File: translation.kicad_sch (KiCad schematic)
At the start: 12 parts, among them Q1 DMG1013UW-7, Q2 DMG1012UW-7, Q3 DMG1012UW-7, U3 TC1262-3.0VDBTR, U4 FXLA108BQX

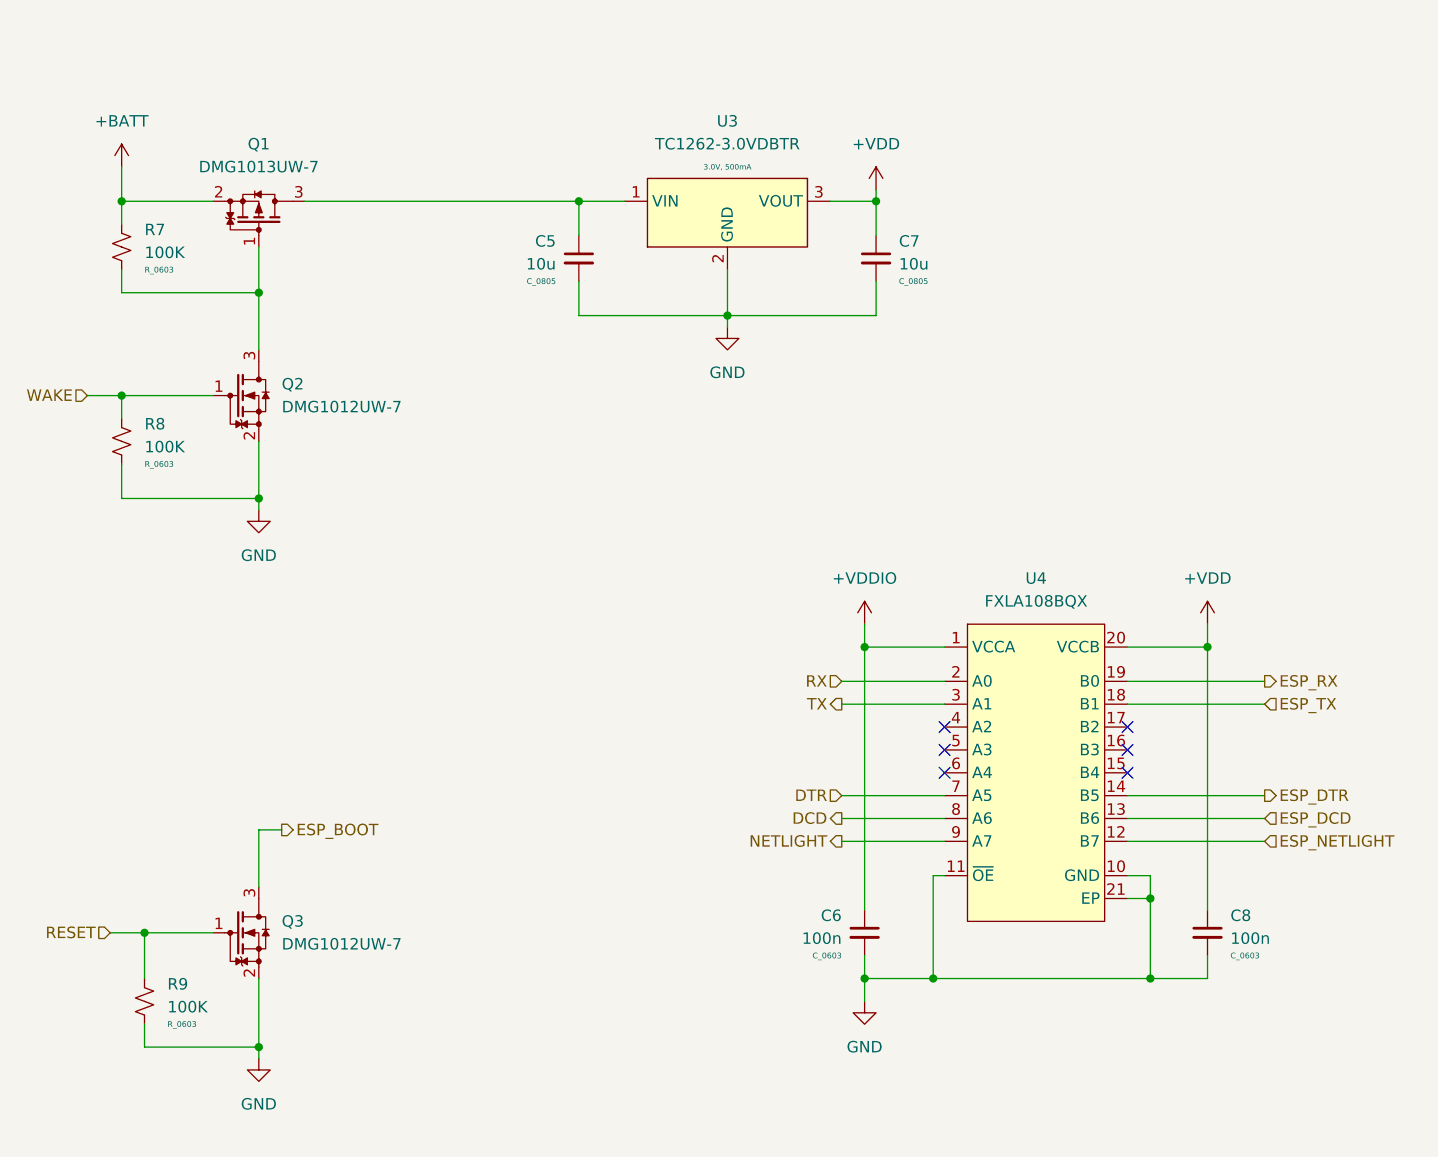
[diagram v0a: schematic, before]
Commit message: Overhaul for buck-boost converter
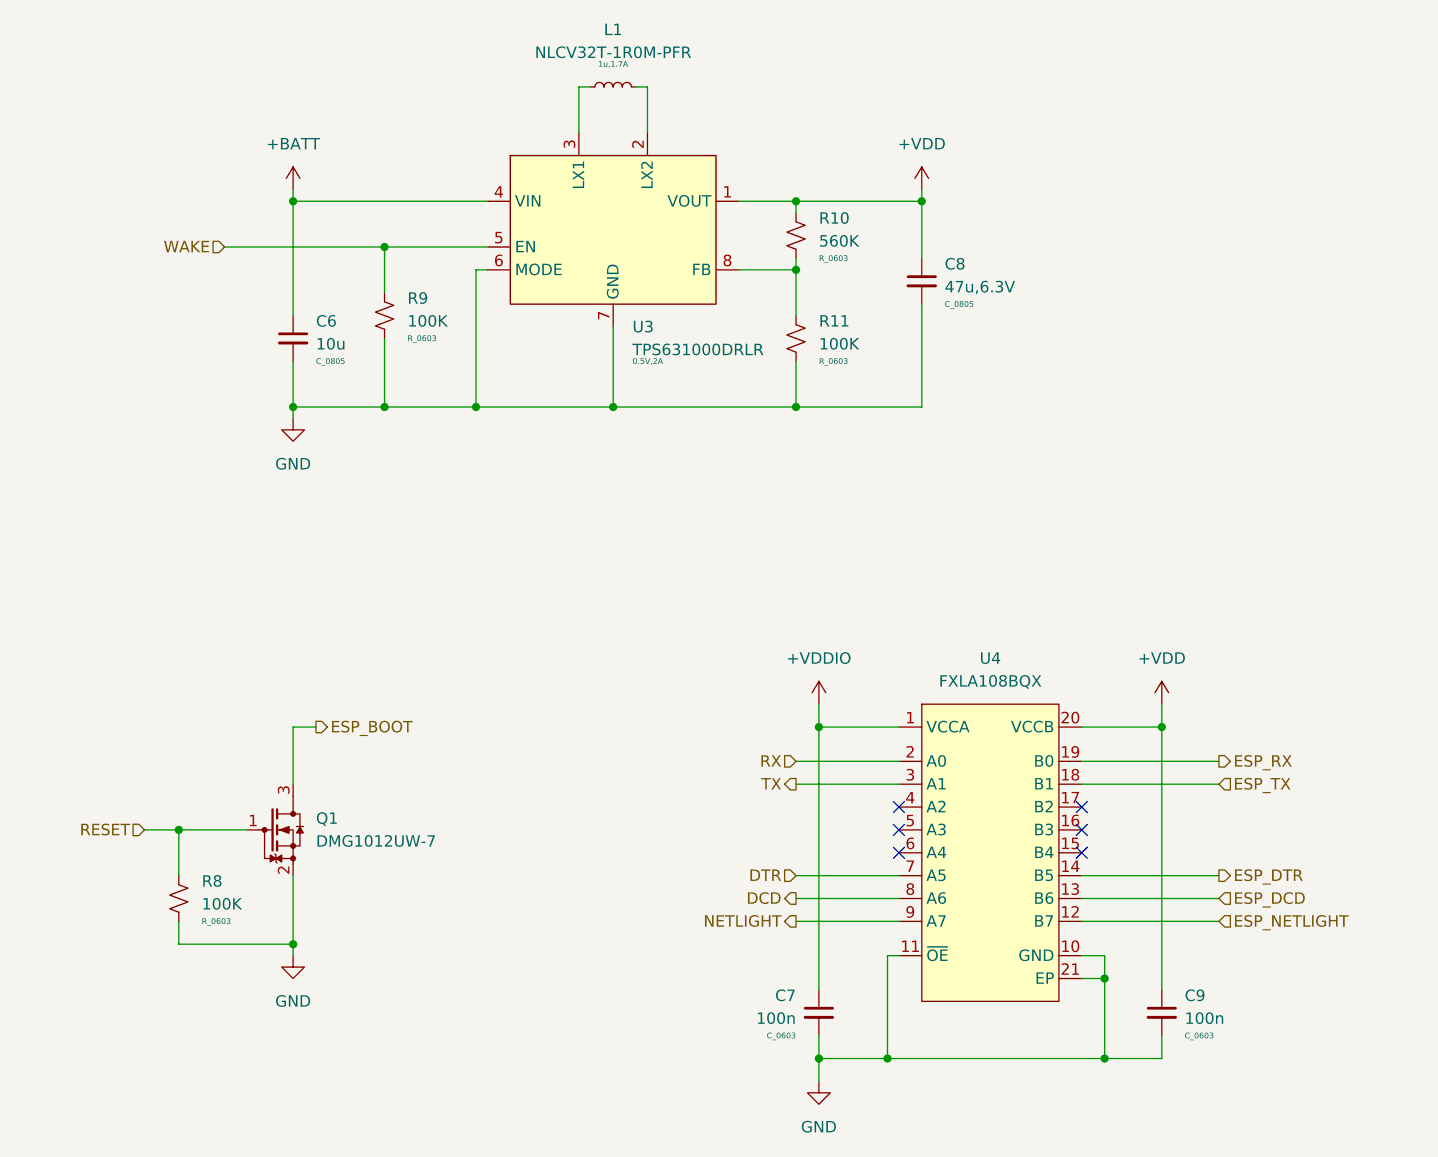
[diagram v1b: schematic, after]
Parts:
- removed C5, C7: 10u, C_Capacitor:C_0805, symbol C_Capacitor:C_0805
- removed Q1: DMG1013UW-7, U_IC:SC70-3, symbol Q_MOSFET:DMG1013UW-7
- removed Q2: DMG1012UW-7, U_IC:SC70-3, symbol Q_MOSFET:DMG1012UW-7
- removed R7: 100K, R_Resistor:R_0603, symbol R_Resistor:R_0603
- removed U3: TC1262-3.0VDBTR, U_IC:SOT223_3, symbol U_Power:TC1262-3.3VDBTR
- added C6: 10u, C_Capacitor:C_0805, symbol C_Capacitor:C_0805
- added C8: 47u,6.3V, C_Capacitor:C_0805, symbol C_Capacitor:C_0805
- added L1: NLCV32T-1R0M-PFR, L_Inductor:L_1210, symbol L_Inductor:NLCV32T-4R7M-PFR
- added R10: 560K, R_Resistor:R_0603, symbol R_Resistor:R_0603
- added R11: 100K, R_Resistor:R_0603, symbol R_Resistor:R_0603
- added U3: TPS631000DRLR, U_IC:SOT583, symbol U_Power:TPS631000
- renumbered C6 to C7, C8 to C9, Q3 to Q1, R9 to R8, R8 to R9
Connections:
- net +BATT: now also C6.1, U3.4 (VIN)
- net +VDD: now also C8.1, R10.1, U3.1 (VOUT)
- net GND: now also C6.2, C8.2, R11.2, U3.6 (MODE), U3.7 (GND)
- net WAKE: now also U3.5 (EN)
- new net: R10.2, R11.1, U3.8 (FB)
- new net: L1.1, U3.3 (LX1)
- new net: L1.2, U3.2 (LX2)
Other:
- company: (none) -> TL Embedded
- title: (none) -> Winglet-ESP
- moved on the sheet: C7, C9, Q1, R8, R9, U4
